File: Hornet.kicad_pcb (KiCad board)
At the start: 2 copper layers, 22.3 x 13 mm, 7 parts, among them J1 Conn_01x04_Female, U1 AP63203WU

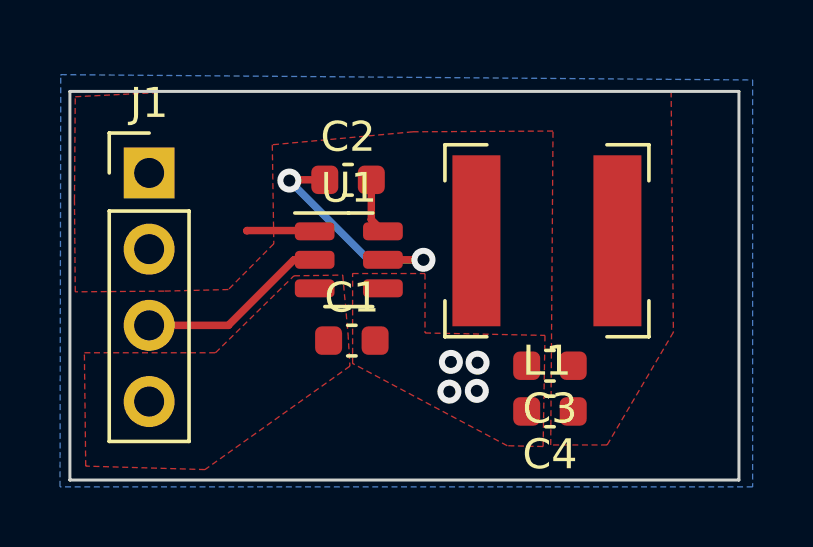
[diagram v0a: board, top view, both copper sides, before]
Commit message: Second layout to make board smaller
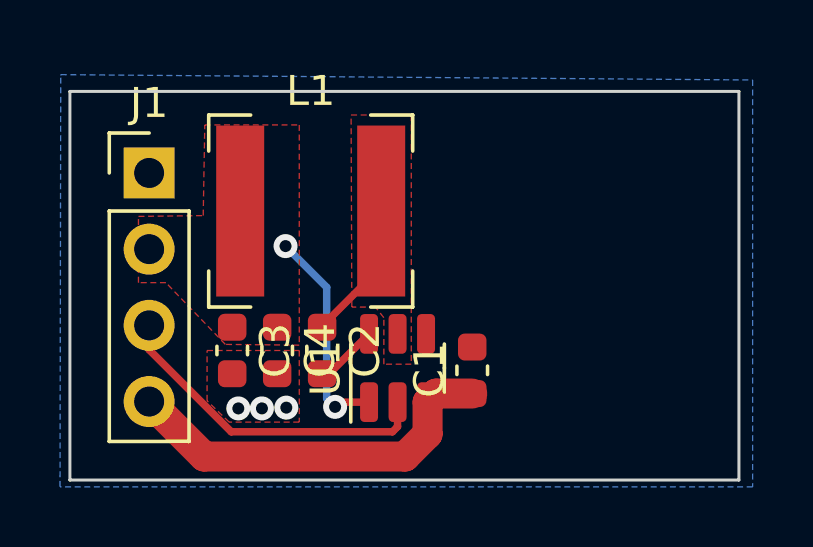
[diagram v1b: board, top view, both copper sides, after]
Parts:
- moved C3 10.6 mm to (123.0, 92.1), turned to -90 degrees
- moved C4 9.32 mm to (124.5, 92.1), turned to -90 degrees
- moved L1 7.94 mm to (125.6, 87.5), turned to 180 degrees
- moved C2 5.75 mm to (126.0, 92.1), turned to -90 degrees
- moved C1 4.13 mm to (131.0, 92.8), turned to 90 degrees
- moved U1 3.96 mm to (128.5, 92.7), turned to 90 degrees
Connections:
- net Net-(C2-Pad1) renamed /SW
- net Net-(C2-Pad2) renamed /BST
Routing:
- net Vin: track 0.12 -> 13.0 mm
- net 3.3v: track 2.28 -> 7.24 mm, vias 0 -> 2
- net EN: track 6.42 -> 11.1 mm
- net /SW: track 8.11 -> 4.69 mm, vias 2 -> 0
- net GND: vias 4 -> 3
- added copper zone on F.Cu, net /SW
- removed copper zone on F.Cu, net Vin

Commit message: New layout and added component part numbers
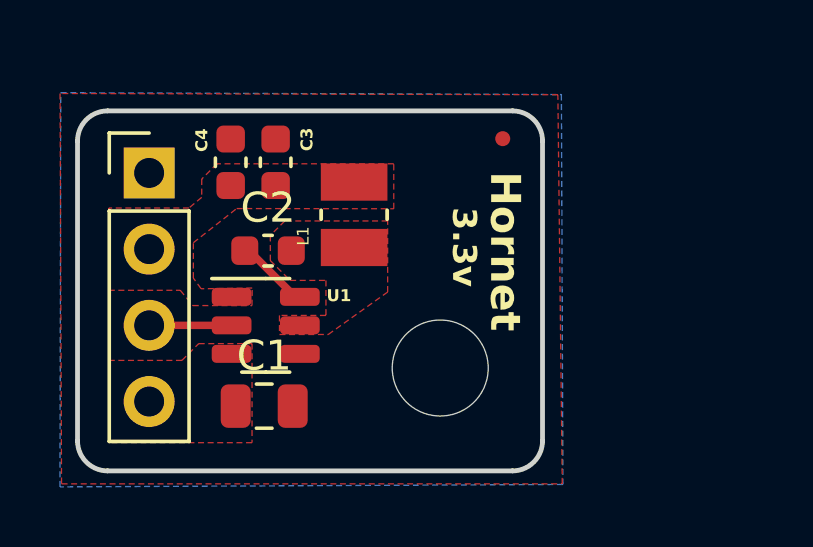
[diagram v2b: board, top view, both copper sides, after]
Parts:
- added FID1: Fiducial, Fiducial:Fiducial_0.5mm_Mask1.5mm, F.Cu at (132.0, 85.1)
- added H1: MountingHole, MountingHole:MountingHole_3.2mm_M3_ISO7380, F.Cu at (129.9, 92.7)
- C1: footprint Capacitor_SMD:C_0603_1608Metric -> Capacitor_SMD:C_0805_2012Metric
- L1: value 3.9uH -> DFE252012P-4R7M=P2; footprint Inductor_SMD:L_Bourns-SRN6028 -> SnapEDA Library:INDC2520X120N
- moved C1 7.04 mm to (124.1, 94.0), turned to 0 degrees
- moved C4 6.46 mm to (122.9, 85.9), turned to 90 degrees
- moved C3 6.44 mm to (124.4, 85.9), turned to 90 degrees
- moved U1 4.62 mm to (124.1, 91.3), turned to 0 degrees
- moved C2 3.78 mm to (124.2, 88.8), turned to 0 degrees
- moved L1 1.45 mm to (127.1, 87.6), turned to 90 degrees
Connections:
- C2 pad 1: /SW -> Net-(U1-BST)
- C2 pad 2: /BST -> /SW
- U1 pad 6: /BST -> Net-(U1-BST)
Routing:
- net Vin: track 13.0 -> 0.00 mm
- net EN: track 11.1 -> 2.60 mm
- net 3.3v: track 7.24 -> 0.00 mm, vias 2 -> 0
- net /SW: track 4.69 -> 0.00 mm
- net Net-(U1-BST): track 0.00 -> 2.30 mm
- net /BST: track 2.11 -> 0.00 mm
- net GND: vias 3 -> 0
- added copper zone on F.Cu, net Vin
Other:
- board size 22.3 x 13 mm -> 15.5 x 12 mm
- board text added: "3.3v"
- board text added: "Hornet"
- board text added: "V0.1 Input: 3.5-32v"
